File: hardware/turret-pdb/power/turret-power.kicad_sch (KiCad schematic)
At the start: 29 parts, among them J1 Battery in, J10 Vision 5V, J11 Servo bus 7.5V, J2 12V bench, J3 Arm switch, J4 Pusher, J5 ESC left, J6 ESC right, J7 TTLinker, J8 TFmini Plus, J9 Light gate, U1 Freenove ESP32-S3 WROOM, U2 Adafruit 757, U3 MP1584 7.5V, U4 MP1584 6V, U5 MP1584 5V

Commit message: Generate the controller board per board name, as the power project
Co-Authored-By: Claude Opus 5.5 <noreply@anthropic.com>
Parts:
- C1: footprint turret-pdb:C_Disc_P5.00mm -> turret-power:C_Disc_P5.00mm; symbol turret-pdb:C -> turret-power:C
- C2: footprint turret-pdb:CP_Radial_D6.3mm_P2.50mm -> turret-power:CP_Radial_D6.3mm_P2.50mm; symbol turret-pdb:C_Polarized -> turret-power:C_Polarized
- C3: footprint turret-pdb:CP_Radial_D10.0mm_P5.00mm -> turret-power:CP_Radial_D10.0mm_P5.00mm; symbol turret-pdb:C_Polarized -> turret-power:C_Polarized
- D1, D2: footprint turret-pdb:D_DO-201AD_P12.70mm_Horizontal -> turret-power:D_DO-201AD_P12.70mm_Horizontal; symbol turret-pdb:D_Schottky -> turret-power:D_Schottky
- H1, H2, H3, H4: footprint turret-pdb:MountingHole_M3 -> turret-power:MountingHole_M3; symbol turret-pdb:MountingHole -> turret-power:MountingHole
- J1, J10, J11: footprint turret-pdb:WirePads_1x02_TieRight -> turret-power:WirePads_1x02_TieRight; symbol turret-pdb:WirePads_01x02 -> turret-power:WirePads_01x02
- J2: footprint turret-pdb:BarrelJack_5.5x2.1_Horizontal -> turret-power:BarrelJack_5.5x2.1_Horizontal; symbol turret-pdb:BarrelJack -> turret-power:BarrelJack
- J3, J7, J8: footprint turret-pdb:PinHeader_1x04_P2.54mm -> turret-power:PinHeader_1x04_P2.54mm; symbol turret-pdb:Conn_01x04 -> turret-power:Conn_01x04
- J4, J9: footprint turret-pdb:PinHeader_1x03_P2.54mm -> turret-power:PinHeader_1x03_P2.54mm; symbol turret-pdb:Conn_01x03 -> turret-power:Conn_01x03
- J5, J6: footprint turret-pdb:PinHeader_1x03_P2.54mm_ESC -> turret-power:PinHeader_1x03_P2.54mm_ESC; symbol turret-pdb:Conn_ESC -> turret-power:Conn_ESC
- R1, R2, R3, R4: footprint turret-pdb:R_Axial_P10.16mm_Horizontal -> turret-power:R_Axial_P10.16mm_Horizontal; symbol turret-pdb:R -> turret-power:R
- U1: footprint turret-pdb:Freenove_ESP32-S3_WROOM_Socket -> turret-power:Freenove_ESP32-S3_WROOM_Socket; symbol turret-pdb:Freenove_ESP32-S3_WROOM -> turret-power:Freenove_ESP32-S3_WROOM
- U2: footprint turret-pdb:Adafruit_757_UpsideDown -> turret-power:Adafruit_757_UpsideDown; symbol turret-pdb:Adafruit_757 -> turret-power:Adafruit_757
- U3, U4, U5: footprint turret-pdb:MP1584_Module -> turret-power:MP1584_Module; symbol turret-pdb:MP1584_Module -> turret-power:MP1584_Module

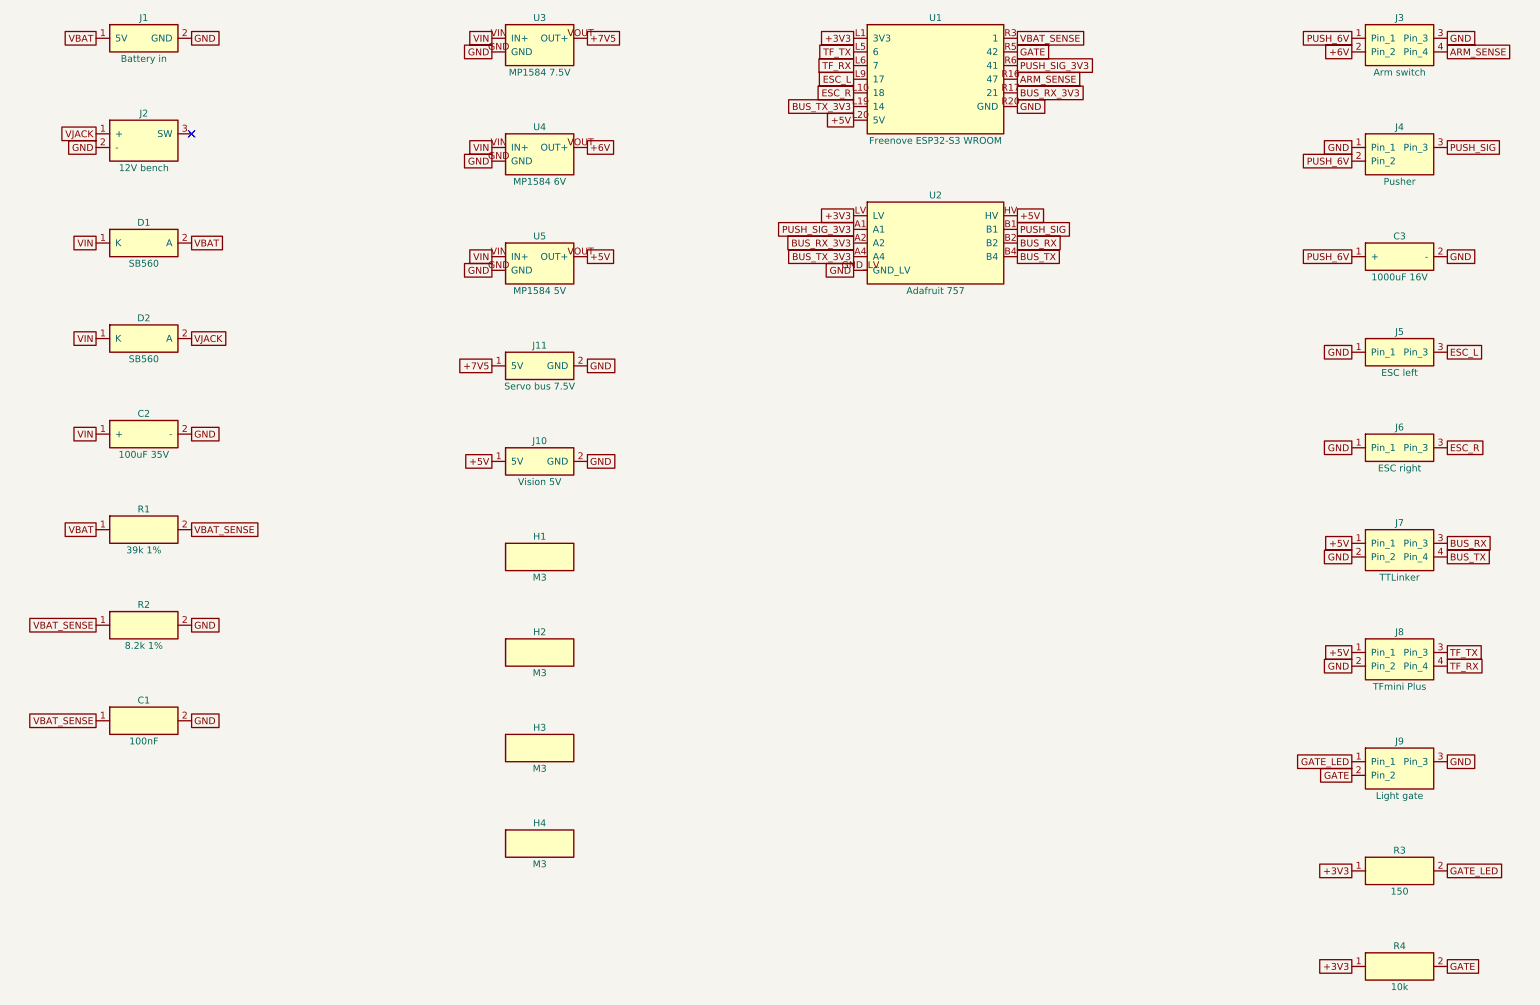
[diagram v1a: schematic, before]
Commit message: Split the controller board into placed power and logic boards
Co-Authored-By: Claude Opus 5.5 <noreply@anthropic.com>
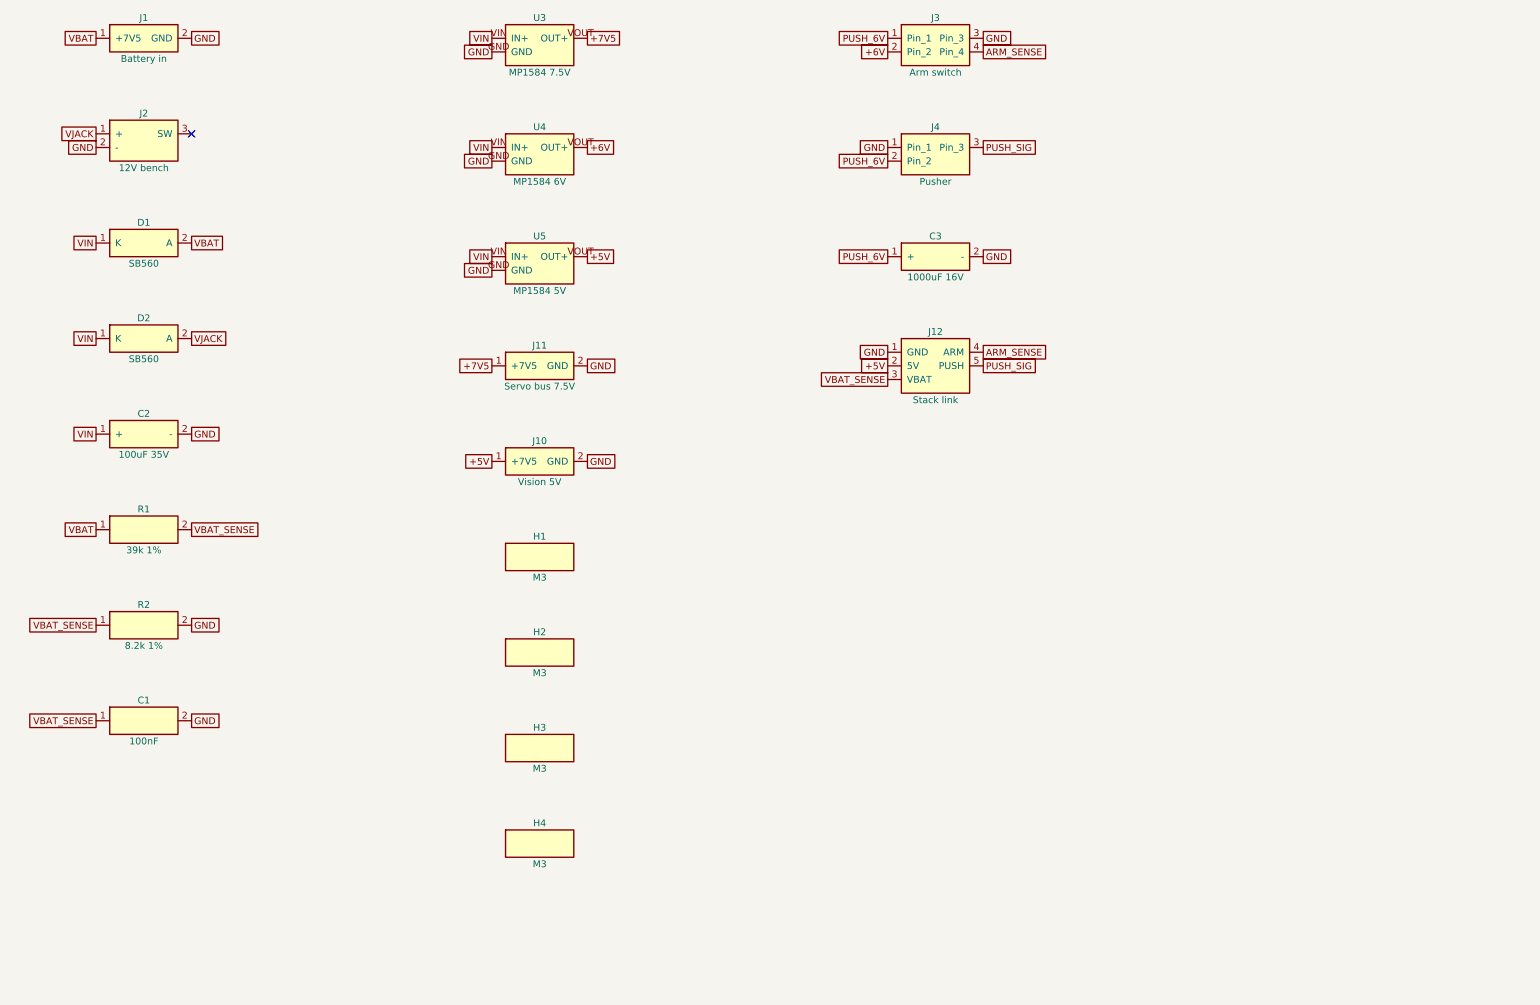
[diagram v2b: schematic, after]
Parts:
- removed J5: ESC left, turret-power:PinHeader_1x03_P2.54mm_ESC, symbol turret-power:Conn_ESC
- removed J6: ESC right, turret-power:PinHeader_1x03_P2.54mm_ESC, symbol turret-power:Conn_ESC
- removed J7: TTLinker, turret-power:PinHeader_1x04_P2.54mm, symbol turret-power:Conn_01x04
- removed J8: TFmini Plus, turret-power:PinHeader_1x04_P2.54mm, symbol turret-power:Conn_01x04
- removed J9: Light gate, turret-power:PinHeader_1x03_P2.54mm, symbol turret-power:Conn_01x03
- removed R3: 150, turret-power:R_Axial_P10.16mm_Horizontal, symbol turret-power:R
- removed R4: 10k, turret-power:R_Axial_P10.16mm_Horizontal, symbol turret-power:R
- removed U1: Freenove ESP32-S3 WROOM, turret-power:Freenove_ESP32-S3_WROOM_Socket, symbol turret-power:Freenove_ESP32-S3_WROOM
- removed U2: Adafruit 757, turret-power:Adafruit_757_UpsideDown, symbol turret-power:Adafruit_757
- added J12: Stack link, turret-power:WirePads_1x05_NoTie, symbol turret-power:WirePads_01x05
- C3: footprint turret-power:CP_Radial_D10.0mm_P5.00mm -> turret-power:CP_Radial_D10.0mm_L20.0mm_P5.00mm_Lying
- J1: footprint turret-power:WirePads_1x02_TieRight -> turret-power:WirePads_1x02_TieLeft
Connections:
- net +5V: now also J12.2 (5V)
- net ARM_SENSE: now also J12.4 (ARM)
- net GND: now also J12.1 (GND)
- net PUSH_SIG: now also J12.5 (PUSH)
- net VBAT_SENSE: now also J12.3 (VBAT)
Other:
- moved on the sheet: C3, J3, J4

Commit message: Route the power board
Co-Authored-By: Claude Opus 5.5 <noreply@anthropic.com>
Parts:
- J10: footprint turret-power:WirePads_1x02_TieRight -> turret-power:WirePads_1x02_NoTie
- J3: footprint turret-power:PinHeader_1x04_P2.54mm -> turret-power:WirePads_1x04_NoTie; symbol turret-power:Conn_01x04 -> turret-power:WirePads_01x04
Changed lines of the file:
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@@
 	)
 	(symbol
-		(lib_id "turret-power:Conn_01x04")
+		(lib_id "turret-power:WirePads_01x04")
 		(at 187.96 34.29 0)
 		(unit 1)
@@
 			)
 		)
-		(property "Footprint" "turret-power:PinHeader_1x04_P2.54mm"
+		(property "Footprint" "turret-power:WirePads_1x04_NoTie"
 			(at 187.96 34.29 0)
 			(effects
@@
 			)
 		)
-		(property "Description" "1x4 2.54 mm male header, pads on the solder side only"
+		(property "Description" "Solder holes for stranded wire, zip-tie holes at both ends for strain relief"
 			(at 187.96 34.29 0)
 			(effects
@@
 			)
 		)
-		(property "Footprint" "turret-power:WirePads_1x02_TieRight"
+		(property "Footprint" "turret-power:WirePads_1x02_NoTie"
 			(at 114.3 111.76 0)
 			(effects

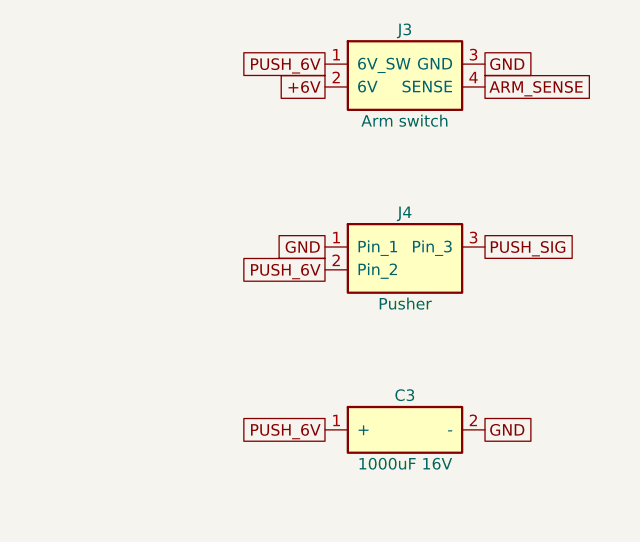
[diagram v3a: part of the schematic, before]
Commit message: Fix review findings: back-side link soldering, J4 solder holes, 17 mm gap
Co-Authored-By: Claude Opus 5.5 <noreply@anthropic.com>
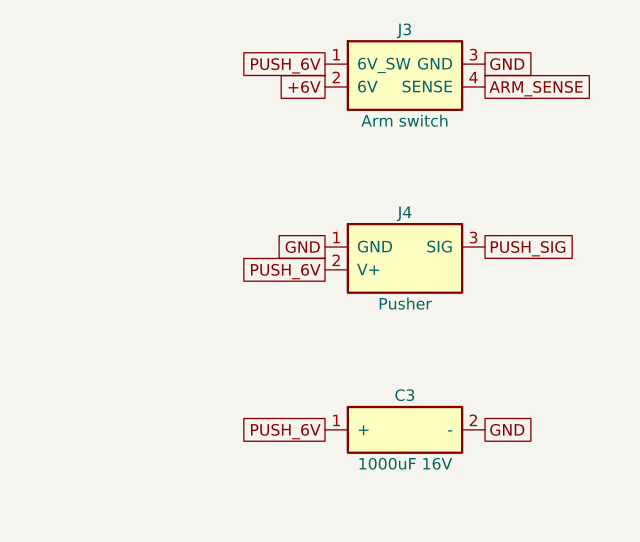
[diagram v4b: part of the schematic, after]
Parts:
- J4: footprint turret-power:PinHeader_1x03_P2.54mm -> turret-power:WirePads_1x03_NoTie; symbol turret-power:Conn_01x03 -> turret-power:WirePads_01x03
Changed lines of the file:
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@@
 			)
 		)
-		(property "Description" "Solder holes for stranded wire, zip-tie holes at both ends for strain relief"
+		(property "Description" "Solder holes for stranded wire, zip-tie holes for strain relief"
 			(at 40.64 33.02 0)
 			(effects
@@
 			)
 		)
-		(property "Description" "Solder holes for stranded wire, zip-tie holes at both ends for strain relief"
+		(property "Description" "Solder holes for stranded wire, zip-tie holes for strain relief"
 			(at 114.3 93.98 0)
 			(effects
@@
 			)
 		)
-		(property "Description" "Solder holes for stranded wire, zip-tie holes at both ends for strain relief"
+		(property "Description" "Solder holes for stranded wire"
 			(at 187.96 34.29 0)
 			(effects
@@
 	)
 	(symbol
-		(lib_id "turret-power:Conn_01x03")
+		(lib_id "turret-power:WirePads_01x03")
 		(at 187.96 54.61 0)
 		(unit 1)
@@
 			)
 		)
-		(property "Footprint" "turret-power:PinHeader_1x03_P2.54mm"
+		(property "Footprint" "turret-power:WirePads_1x03_NoTie"
 			(at 187.96 54.61 0)
 			(effects
@@
 			)
 		)
-		(property "Description" "1x3 2.54 mm male header, pads on the solder side only"
+		(property "Description" "Solder holes for stranded wire"
 			(at 187.96 54.61 0)
 			(effects
@@
 			)
 		)
-		(property "Description" "Solder holes for stranded wire, zip-tie holes at both ends for strain relief"
+		(property "Description" "Solder holes for stranded wire"
 			(at 114.3 111.76 0)
 			(effects
@@
 			)
 		)
-		(property "Description" "Solder holes for stranded wire, zip-tie holes at both ends for strain relief"
+		(property "Description" "Solder holes for stranded wire"
 			(at 187.96 93.98 0)
 			(effects
